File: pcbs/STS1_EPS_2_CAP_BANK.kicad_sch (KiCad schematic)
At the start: 16 parts

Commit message: Fixed some warnings and errors.
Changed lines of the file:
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@@
 	)
 	(hierarchical_label "BACKED_V"
-		(shape output)
+		(shape passive)
 		(at 226.06 27.94 0)
 		(fields_autoplaced yes)
@@
 	)
 	(hierarchical_label "INTERNAL_V"
-		(shape input)
+		(shape passive)
 		(at 30.48 27.94 180)
 		(fields_autoplaced yes)
@@
 			)
 		)
-		(property "Description" ""
+		(property "Description" "Power symbol creates a global label with name \"GND\" , ground"
 			(at 109.855 70.485 0)
 			(effects
@@
 			)
 		)
-		(property "Description" ""
+		(property "Description" "Power symbol creates a global label with name \"GND\" , ground"
 			(at 65.405 70.485 0)
 			(effects
@@
 			)
 		)
-		(property "Description" ""
+		(property "Description" "Power symbol creates a global label with name \"GND\" , ground"
 			(at 39.37 45.085 0)
 			(effects
@@
 			)
 		)
-		(property "Description" ""
+		(property "Description" "Power symbol creates a global label with name \"GND\" , ground"
 			(at 56.515 70.485 0)
 			(effects
@@
 			)
 		)
-		(property "Description" ""
+		(property "Description" "Power symbol creates a global label with name \"GND\" , ground"
 			(at 83.185 70.485 0)
 			(effects
@@
 			)
 		)
-		(property "Description" ""
+		(property "Description" "Power symbol creates a global label with name \"GND\" , ground"
 			(at 113.665 45.085 0)
 			(effects
@@
 			)
 		)
-		(property "Description" ""
+		(property "Description" "Power symbol creates a global label with name \"GND\" , ground"
 			(at 120.015 70.485 0)
 			(effects
@@
 			)
 		)
-		(property "Description" ""
+		(property "Description" "Power symbol creates a global label with name \"GND\" , ground"
 			(at 92.075 70.485 0)
 			(effects
@@
 			)
 		)
-		(property "Description" ""
+		(property "Description" "Power symbol creates a global label with name \"GND\" , ground"
 			(at 129.54 70.485 0)
 			(effects
@@
 			)
 		)
-		(property "Description" ""
+		(property "Description" "Power symbol creates a global label with name \"GND\" , ground"
 			(at 47.625 70.485 0)
 			(effects
@@
 			)
 		)
-		(property "Description" ""
+		(property "Description" "Power symbol creates a global label with name \"GND\" , ground"
 			(at 58.42 45.085 0)
 			(effects
@@
 			)
 		)
-		(property "Description" ""
+		(property "Description" "Power symbol creates a global label with name \"GND\" , ground"
 			(at 39.37 70.485 0)
 			(effects
@@
 			)
 		)
-		(property "Description" ""
+		(property "Description" "Power symbol creates a global label with name \"GND\" , ground"
 			(at 74.295 70.485 0)
 			(effects
@@
 			)
 		)
-		(property "Description" ""
+		(property "Description" "Power symbol creates a global label with name \"GND\" , ground"
 			(at 100.965 70.485 0)
 			(effects
@@
 			)
 		)
-		(property "Description" ""
+		(property "Description" "Power symbol creates a global label with name \"GND\" , ground"
 			(at 77.47 45.085 0)
 			(effects
@@
 			)
 		)
-		(property "Description" ""
+		(property "Description" "Power symbol creates a global label with name \"GND\" , ground"
 			(at 95.885 45.085 0)
 			(effects

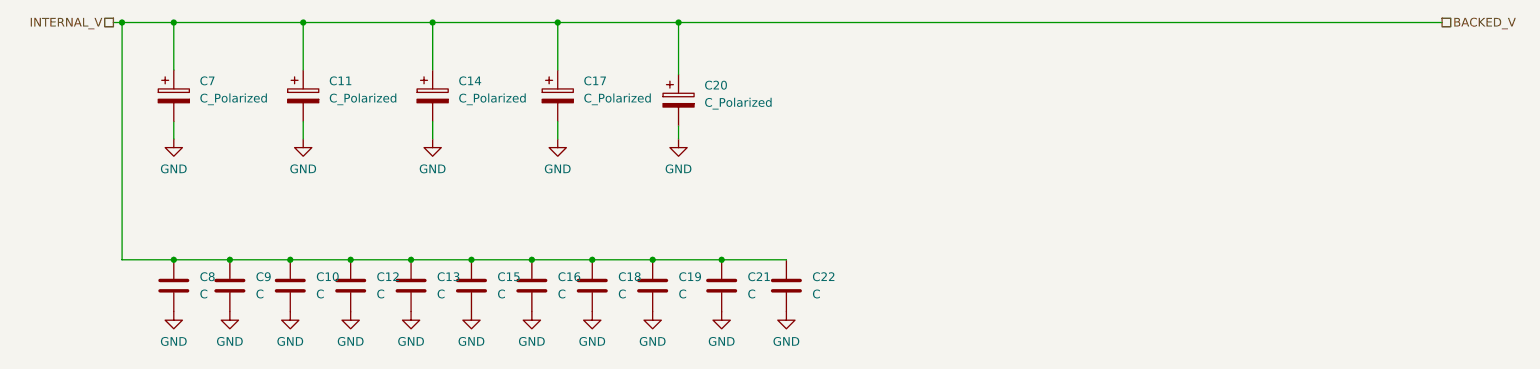
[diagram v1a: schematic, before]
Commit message: Fixed warnings and errors.
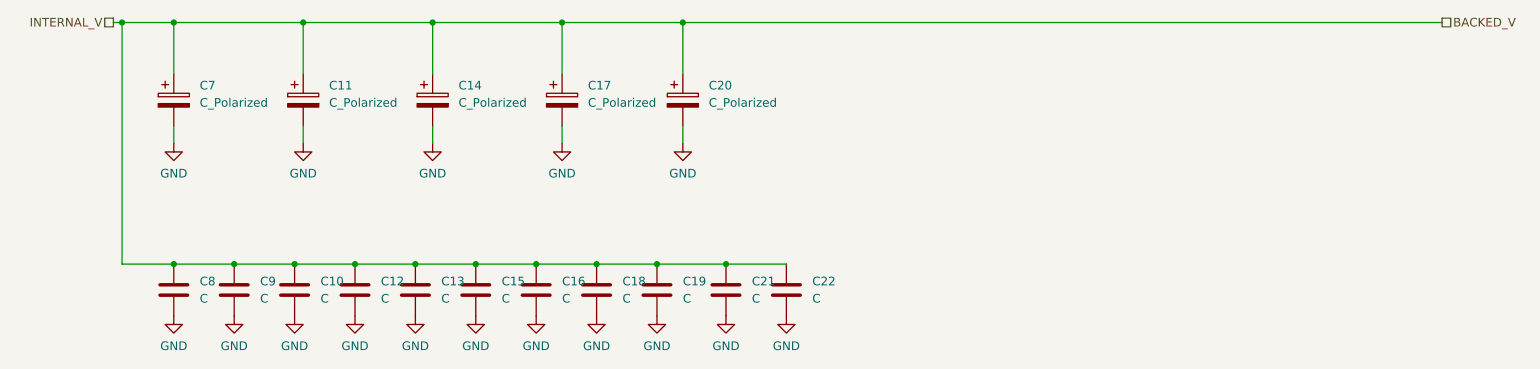
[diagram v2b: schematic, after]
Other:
- moved on the sheet: C10, C11, C12, C13, C14, C15, C16, C17, C18, C19, C20, C21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
